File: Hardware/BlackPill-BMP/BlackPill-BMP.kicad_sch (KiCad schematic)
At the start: 41 parts, among them J1 JTAG, J10 Conn_01x12_Male, J2 VCC, J3 GND, J4 SWO, J5 GDB_COMM, J6 TVCC, J7 LogicAna, J8 Conn_01x06_Male, J9 Conn_01x05_Male, U1 BlueAndBlackPill, U2 AD8531ARTZ, U3 74LVC2T45DC, U4 74LS125, U5 74LS125, U6 SRV05-4, U7 SRV05-4

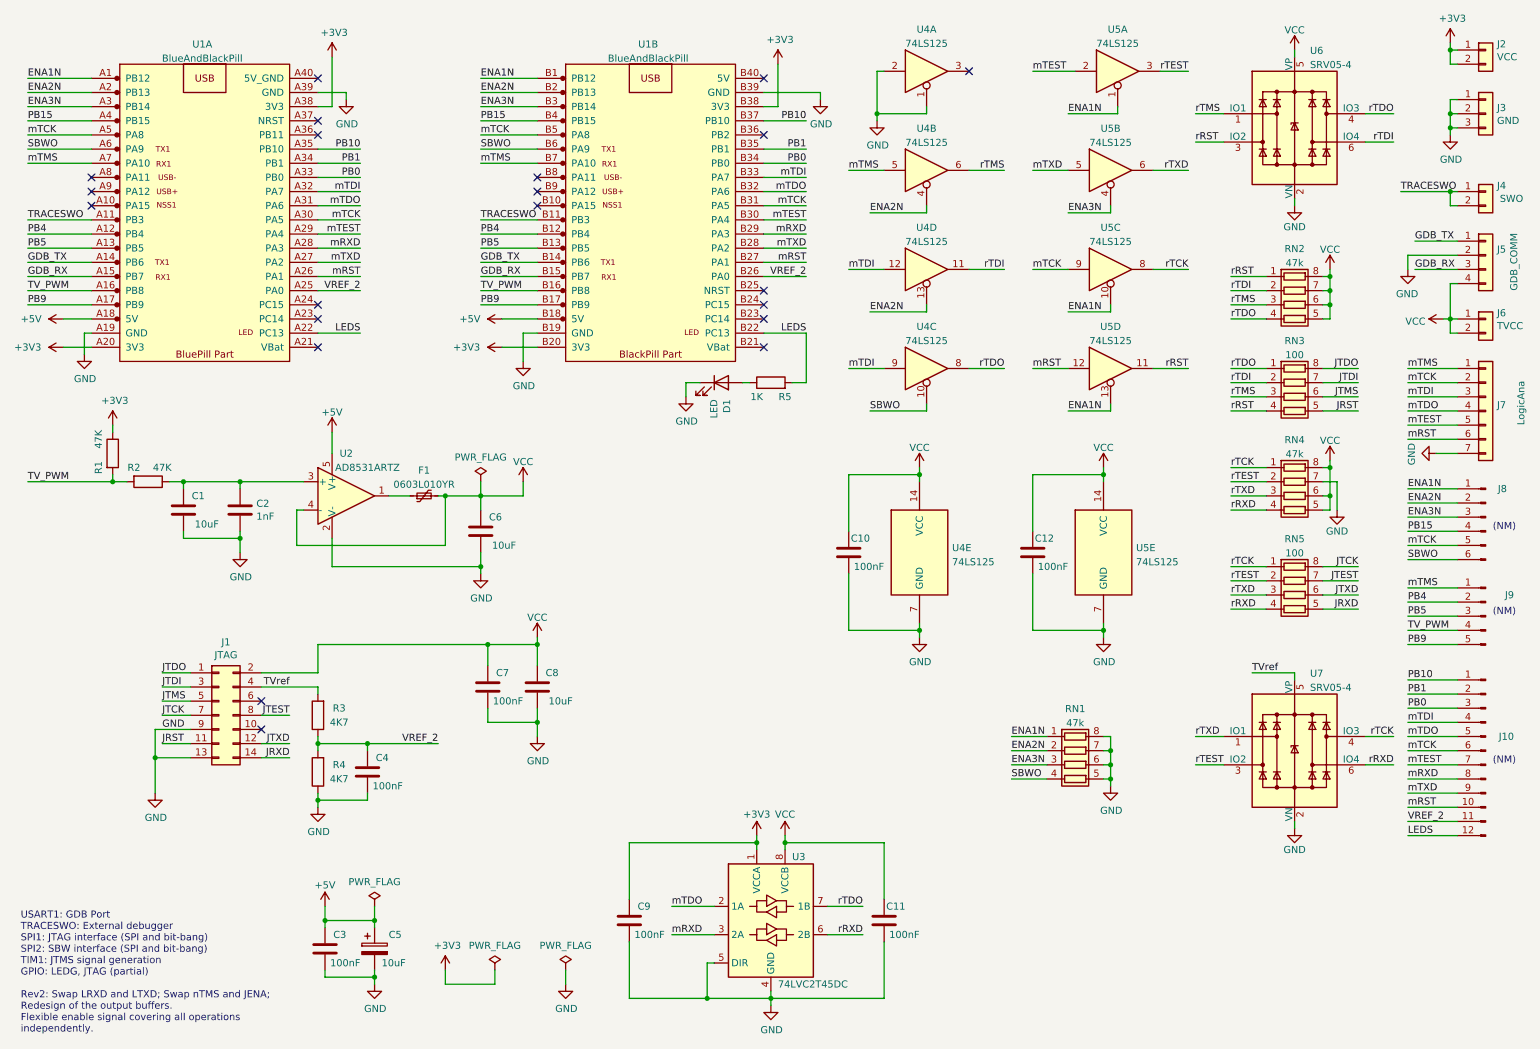
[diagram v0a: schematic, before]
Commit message: Updated BOM on the schematics for the BluePill/BlackPill design (no PCB or fabrication changes).
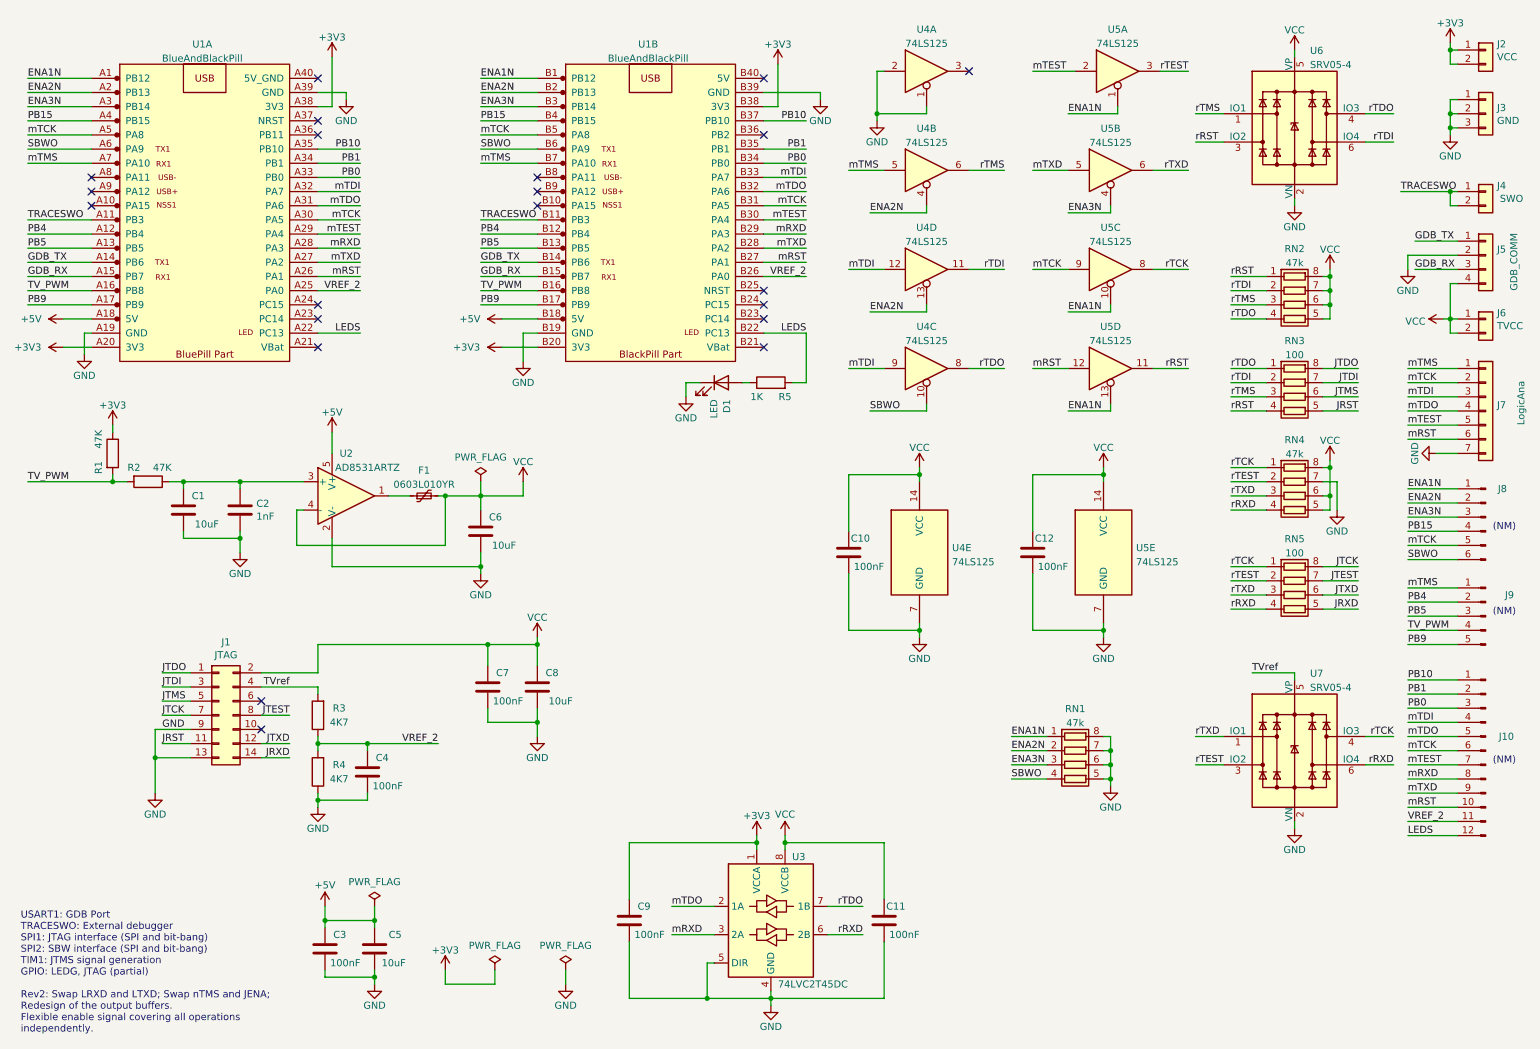
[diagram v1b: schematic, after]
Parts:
- C1, C6, C8: MOUSER (none) -> 81-GRM188Z71A106KA3D
- C10, C11, C12, C3, C4, C7, C9: MOUSER (none) -> 187-CL10B104KA85PNC
- C2: MOUSER (none) -> 791-MT18N102J500CT
- C5: symbol Device:C_Polarized -> Device:C; MOUSER (none) -> 81-GRM188Z71A106KA3D
- D1: MOUSER (none) -> 710-151053GS03000
- F1: MOUSER (none) -> 576-0603L010YR
- J1: MOUSER (none) -> 710-61201421621
- J10: MOUSER (none) -> 517-2312-6111TG
- J2, J4, J6: MOUSER (none) -> 571-146280-2
- J3: MOUSER (none) -> 571-873483
- J5: MOUSER (none) -> 538-171856-1004
- J7: MOUSER (none) -> 571-872247
- J8: MOUSER (none) -> 571-87348-6
- J9: MOUSER (none) -> 571-872245
- R1, R2: MOUSER (none) -> 603-RT0603FRE1347KL
- R3, R4: MOUSER (none) -> 603-AC0603FR-7W4K7L
- R5: MOUSER (none) -> 603-RT0603FRE071KL
- RN1, RN2, RN4: MOUSER (none) -> 667-EXB-28V473JX
- RN3, RN5: MOUSER (none) -> 667-EXB-28V101JX
- U1: MOUSER (none) -> 855-M20-7832046
- U2: MOUSER (none) -> 584-AD8531ARTZ-R
- U3: MOUSER (none) -> 771-AVCH2T45DC125
- U4, U5: MOUSER (none) -> 771-74LVC125APWQ100J
- U6, U7: MOUSER (none) -> 576-SRV05-4HTG-D

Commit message: BluePill/BlackPill Prototype: Fixed LED part number
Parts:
- D1: MOUSER 710-151053GS03000 -> 710-151053RS03000
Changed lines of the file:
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@@
       (effects (font (size 1.27 1.27)) hide)
     )
-    (property "MOUSER" "710-151053GS03000" (id 4) (at 139.7 80.01 0)
+    (property "MOUSER" "710-151053RS03000" (id 4) (at 139.7 80.01 0)
       (effects (font (size 1.27 1.27)) hide)
     )
